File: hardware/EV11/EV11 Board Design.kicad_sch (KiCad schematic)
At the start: 121 parts, among them CN1 PJ-313E-8A_C707222, CN2 X1270WVS-2X05B-6TV01, CN3 WAFER-SH1.0-6PWB, CN4 WAFER-SH1.0-6PWB, CN5 Conn_05x02_Male, CN6 Conn_05x02_Male, CN7 Conn_05x02_Male, J1 Conn_01x02_Socket, J10 Conn_01x08_Socket, J9 USB_C_Receptacle, SW1 TS-1037-A11B3-D2, SW3 TS-1037-A11B3-D2, SW4 SW_Push, SW5 SW_Push, SW6 SW_SPDT, U1 STM32F405RGTx, U11 ESP32-S3-WROOM-1-N8R2, U13 BM14B(0.8)-24DS-0.4V(53), U3 CH340C, U4 USBLC6-2P6, U5 M24C02-RMN6TP, U6 WM8960CGEFL/RV, U7 TPS63060, U8 STM32F072C8T6, U9 BQ21040DBV, Y1 Crystal_GND24

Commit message: Updated vias to be .6mm/.3mm. Added Analog plane. Added more debug connectors
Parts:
- removed CN1: PJ-313E-8A_C707222, PJ-313E-8A:AUDIO-SMD_PJ-313E-8A-EH, symbol PJ-313E-8A:PJ-313E-8A_C707222
- removed U11: ESP32-S3-WROOM-1-N8R2, RF_Module:ESP32-S3-WROOM-1U, symbol ESP32-S3-WROOM-1-N8R2:ESP32-S3-WROOM-1-N8R2
- removed U8: STM32F072C8T6, STM32F072C8T6:LQFP-48_L7.0-W7.0-P0.50-LS9.0-BL, symbol STM32F072C8T6:STM32F072C8T6
- added C21, C22, C27, C56: 100n, Capacitor_SMD:C_0402_1005Metric, symbol Device:C
- added C33, C52: 4u7, Capacitor_SMD:C_0402_1005Metric, symbol Device:C
- added C49, C50: 1u, Capacitor_SMD:C_0402_1005Metric, symbol Device:C
- added C51, C55: 4.7u, Capacitor_SMD:C_0402_1005Metric, symbol Device:C
- added C53, C54: 100u, Capacitor_SMD:C_1206_3216Metric, symbol Device:C
- added J2: AudioJack1, Connector_Audio:Jack_3.5mm_PJ320D_Horizontal, symbol Connector_Audio:AudioJack4
- added J3: Conn_01x06_Socket, Connector_JST:JST_SHL_SM06B-SHLS-TF_1x06-1MP_P1.00mm_Horizontal, symbol Connector:Conn_01x06_Socket
- added JP2: SolderJumper_2_Bridged, NetTie:NetTie-2_SMD_Pad0.5mm, symbol Jumper:SolderJumper_2_Bridged
- added NT1: NetTie_4, NetTie:NetTie-4_SMD_Pad0.5mm, symbol Device:NetTie_4
- added R42: 0R1, Resistor_SMD:R_0603_1608Metric, symbol Device:R_US
- added R43: 2k2, Resistor_SMD:R_0402_1005Metric, symbol Device:R_US
- added TP1, TP2: TestPoint, TestPoint:TestPoint_THTPad_D1.5mm_Drill0.7mm, symbol Connector:TestPoint
- added U11: ESP32-S3-WROOM-1-N8R2, RF_Module:ESP32-S3-WROOM-1U, symbol RF_Module:ESP32-S3-WROOM-1
- added U8: STM32F070CBTx, Package_QFP:LQFP-48_7x7mm_P0.5mm, symbol MCU_ST_STM32F0:STM32F070CBTx
- added U9: WM8960CGEFL/RV, Package_DFN_QFN:QFN-32-1EP_5x5mm_P0.5mm_EP3.45x3.45mm_ThermalVias, symbol Hactar_Symbols:WM8960CGEFL/RV_1
- CN2: value X1270WVS-2X05B-6TV01 -> Conn_05x02_Female; footprint X1270WVS-2x05B-6TV01:IDC-SMD_10P-P1.27_X1270WVS-2X05B-6TV01 -> Hactar_Footprints:IDC-SMD_10P-P1.27_X1270WVS-2X05B-6TV01; symbol X1270WVS-2x05B-6TV01:X1270WVS-2X05B-6TV01 -> Connector_Generic:Conn_02x05_Odd_Even
- CN3, CN4: value WAFER-SH1.0-6PWB -> Conn_01x06_Female; footprint WAFER-SH1.0-6PWB:CONN-SMD_6P-P1.00_XUNPU_WAFER-SH1.0-6PWB -> Connector_JST:JST_SHL_SM06B-SHLS-TF_1x06-1MP_P1.00mm_Horizontal; symbol WAFER-SH1.0-6PWB:WAFER-SH1.0-6PWB -> Connector:Conn_01x06_Socket
- CN5, CN6, CN7: value Conn_05x02_Male -> Conn_02x05_Male; footprint X1270WVS-2x05B-6TV01:IDC-SMD_10P-P1.27_X1270WVS-2X05B-6TV01 -> Hactar_Footprints:IDC-SMD_10P-P1.27_X1270WVS-2X05B-6TV01; symbol X1270WVS-2x05B-6TV01:X1270WVS-2X05B-6TV01 -> Connector_Generic:Conn_02x05_Odd_Even
- D3, D4, D5, D7: footprint NH-B1515RGBA-HF:LED-ARRAY-SMD_4P-L1.6-W1.5-TL_NH-B1515RGBA -> Hactar_Footprints:LED-ARRAY-SMD_4P-L1.6-W1.5-TL_NH-B1515RGBA; symbol NH-B1515RGBA-HF:NH-B1515RGBA-HF -> Hactar_Symbols:NH-B1515RGBA-HF
- L1: footprint MCL2016A1R0MT:L0806 -> Hactar_Footprints:MCL2016A1R0MT
- R11, R12, R15, R17, R18, R24, R25: value 150 -> 150R
- R16, R23: value 180 -> 180R
- R35: footprint Resistor_SMD:R_0603_1608Metric -> Resistor_SMD:R_0402_1005Metric; JLCPCB Part # C4211 -> C25784
- SW1, SW3: footprint TS-1037-A11B3-D2:KEY-SMD_2P-L7.1-W10.6-P4.00-LS9.0 -> Hactar_Footprints:KEY-SMD_2P-L7.1-W10.6-P4.00-LS9.0; symbol TS-1037-A11B3-D2:TS-1037-A11B3-D2 -> Switch:SW_Push
- SW6: footprint (none) -> Button_Switch_THT:SW_E-Switch_EG1224_SPDT_Angled; JLCPCB Part # (none) -> C273395; JLCPCB Position Offset (none) -> 0.1, 4.1
- U13: footprint BM14B(0.B)-24DS-0:BM14B(0.B)-24DS-0.4V(53) -> Hactar_Footprints:BM14B(0.B)-24DS-0.4V(53); symbol Keyboard Symbol:BM14B(0.8)-24DS-0.4V(53) -> Hactar_Symbols:BM14B(0.8)-24DS-0.4V(53)
- U6: footprint Package_DFN_QFN:QFN-32-1EP_5x5mm_P0.5mm_EP3.3x3.3mm_ThermalVias -> Package_DFN_QFN:QFN-32-1EP_5x5mm_P0.5mm_EP3.45x3.45mm_ThermalVias; symbol Audio Interface:WM8960CGEFL/RV -> Hactar_Symbols:WM8960CGEFL/RV_1
- renumbered U9 to U2
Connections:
- net +3.3V: now also C24.2, C25.2, C26.2, CN5.1 (Pin_1), CN6.1 (Pin_1), SW4.1, U1.1 (VBAT), C21.2, C22.2, C56.1, J3.1 (Pin_1), U11.2 (3V3), U8.1 (VDD), U8.24 (VDD), U8.36 (VDD), U8.48 (VDD), U8.9 (VDDA), U9.10 (DBVDD), U9.8 (DCVDD); no longer C24.1, C25.1, C26.1, CN5.8, CN6.8, SW4.2
- net +3.3VA: now also C27.2, C33.1, C52.1, U9.21 (SPKVDD2), U9.26 (SPKVDD1), U9.32 (AVDD)
- net BOOT1: now also U8.45 (PB8)
- net GND: now also C24.1, C25.1, C26.1, C35.2, CN5.3 (Pin_3), CN6.3 (Pin_3), R2.1, R3.1, R32.2, SW5.1, C21.1, C22.1, C51.2, C55.2, C56.2, J3.6 (Pin_6), JP2.2 (B), NT1.1, NT1.3, U11.1 (GND), U11.40 (GND), U11.41 (GND), U8.23 (VSS), U8.35 (VSS), U8.47 (VSS), U8.8 (VSSA), U9.20 (SPKGND2), U9.24 (SPKGND1), U9.28 (AGND), U9.33 (EP), U9.9 (DGND); no longer C24.2, C25.2, C26.2, C28.2, C3.2, C31.1, C35.1, C6.2, C7.1, C8.2, C9.2, CN5.10, CN6.10, JP1.2 (B), R2.2, R3.2, R32.1, SW5.2, U6.20 (SPKGND2), U6.24 (SPKGND1), U6.28 (AGND), U6.33 (EP)
- net HP_L: now also C53.2, J2.T
- net HP_R: now also C54.2, J2.R1
- net I2S_ADCDAT: now also CN5.10 (Pin_10), U9.16 (ADCDAT); no longer CN5.5
- net I2S_BCLK: now also CN5.7 (Pin_7), U9.12 (BCLK); no longer CN5.3
- net I2S_DACDAT: now also CN5.8 (Pin_8), U9.14 (DACDAT); no longer CN5.7
- net I2S_DACLRC: now also CN5.9 (Pin_9), U9.13 (DACLRC); no longer CN5.1
- net LEDA_B: now also U8.17 (PA7)
- net LEDA_G: now also U8.16 (PA6)
- net LEDA_R: now also U8.14 (PA4)
- net LEDB_B: now also U8.28 (PB15)
- net LEDB_G: now also U8.27 (PB14)
- net LEDB_R: now also U8.18 (PB0)
- net MCLK: now also CN5.2 (Pin_2), U8.29 (PA8), U9.11 (MCLK); no longer CN5.9
- net MGMT_BOOT: now also SW4.2, U8.44 (BOOT0); no longer SW4.1
- net MGMT_NRST: now also C35.1, SW5.2, U8.7 (NRST); no longer C35.2, SW5.1
- net MGMT_SWCLK: now also U8.37 (PA14)
- net MGMT_SWDIO: now also U8.34 (PA13)
- net MIC_N: now also C5.2, C50.1, J2.R2, JP2.1 (A); no longer C5.1
- net MIC_P: now also C18.2, R9.1, C49.1, J2.S, R43.2; no longer C18.1, R9.2
- net NET_BOOT: now also J3.5 (Pin_5), U11.27 (IO0), U8.41 (PB5)
- net NET_DEBUG_1: now also U11.7 (IO7)
- net NET_DEBUG_2: now also U11.8 (IO15)
- net NET_DEBUG_3: now also U11.9 (IO16)
- net NET_LED_B: now also U11.29 (IO36)
- net NET_LED_G: now also U11.30 (IO37)
- net NET_LED_R: now also U11.31 (IO38)
- net NET_MTCK: now also CN2.6 (Pin_6), U11.32 (IO39); no longer CN2.4
- net NET_MTDI: now also CN2.2 (Pin_2), U11.34 (IO41); no longer CN2.8
- net NET_MTDO: now also CN2.4 (Pin_4), U11.33 (IO40); no longer CN2.6
- net NET_MTMS: now also CN2.8 (Pin_8), U11.35 (IO42); no longer CN2.2
- net NET_NRST: now also J3.2 (Pin_2), U11.3 (EN), U8.40 (PB4)
- net NET_RX1_MGMT: now also CN6.8 (Pin_8), J3.3 (Pin_3), U11.36 (RXD0), U8.21 (PB10); no longer CN6.7
- net NET_STAT: now also U11.23 (IO21), U8.11 (PA1)
- net NET_TX1_MGMT: now also CN6.10 (Pin_10), J3.4 (Pin_4), U11.37 (TXD0), U8.22 (PB11); no longer CN6.9
- net RCC_OSC_IN: now also U8.5 (PF0)
- net RCC_OSC_OUT: now also U8.6 (PF1)
- net UI_BOOT: now also U8.39 (PB3)
- net UI_DEBUG_1: now also U1.44 (PA11); no longer U1.20 (PA4)
- net UI_DEBUG_3: now also U1.20 (PA4); no longer U1.44 (PA11)
- net UI_LED_G: now also R25.1; no longer R24.1
- net UI_LED_R: now also R24.1; no longer R25.1
- net UI_NRST: now also U8.38 (PA15)
- net UI_RX1_MGMT: now also CN6.4 (Pin_4), U8.12 (PA2); no longer CN6.3
- net UI_RX2_NET: now also CN6.7 (Pin_7), U11.10 (IO17); no longer CN6.4
- net UI_SCL: now also CN5.6 (Pin_6), U9.17 (SCLK); no longer CN5.2
- net UI_SDA: now also U9.18 (SDIN)
- net UI_STAT: now also U8.10 (PA0)
- net UI_TX1_MGMT: now also CN6.6 (Pin_6), U8.13 (PA3); no longer CN6.5
- net UI_TX2_NET: now also CN6.5 (Pin_5), U11.11 (IO18); no longer CN6.2
- net USB_CC1_DETECT: now also U1.11 (PC3); no longer U1.10 (PC2)
- net USB_CC2_DETECT: now also U1.10 (PC2); no longer U1.11 (PC3)
- net USB_DTR: now also U8.26 (PB13)
- net USB_RTS: now also U8.19 (PB1)
- net USB_RX1_MGMT: now also CN6.2 (Pin_2), U8.30 (PA9); no longer CN6.1
- net USB_TX1_MGMT: now also CN6.9 (Pin_9), U8.31 (PA10); no longer CN6.6
- net at R36.2: now also CN7.6 (Pin_6); no longer CN7.5
- net at U6.4 (LINPUT1): now also C5.1; no longer C5.2
- net at D7.1 (-): now also R24.2; no longer R25.2
- net at D7.4 (-): now also R25.2; no longer R24.2
- net at R38.2: now also CN7.10 (Pin_10); no longer CN7.1
- net at C37.1, C38.1, C39.1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: now also R42.2, TP2.1; no longer D2.1 (K), D6.1 (K)
- net at C28.1, U6.1 (MICBIAS): now also R9.2; no longer R9.1
- net at U6.27 (AMID): now also C31.1; no longer C31.2
- net at U6.3 (LINPUT2): now also C18.1; no longer C18.2
- net at R41.2: now also CN7.9 (Pin_9); no longer CN7.10
- net at CN7.3 (Pin_3): no longer R37.2
- net at R39.2: now also CN7.5 (Pin_5); no longer CN7.6
- net at CN7.7 (Pin_7): now also R40.2
- net at CN7.8 (Pin_8): now also R37.2; no longer R40.2
- net PG: no longer names the net of R21.1, U7.5 (PG)
- net UD+: no longer names the net of U4.6 (I/O1)
- net UD+: now also J9.A7 (D-), J9.B7 (D-); no longer U3.5 (UD+)
- net UD-: no longer names the net of U4.4 (I/O2)
- net UD-: now also J9.A6 (D+), J9.B6 (D+); no longer U3.6 (UD-)
- removed net USB_D+: J9.A6 (D+), J9.B6 (D+), U4.1 (I/O1)
- removed net USB_D-: J9.A7 (D-), J9.B7 (D-), U4.3 (I/O2)
- new net: C54.1, U9.29 (HP_R)
- new net: C51.1, R43.1, U9.1 (MICBIAS)
- new net: D2.1 (K), D6.1 (K), R42.1, TP1.1
- new net: C50.2, U9.4 (LINPUT1)
- new net: J9.A5 (CC1), R3.2, R31.2
- new net: J9.B5 (CC2), R2.2, R33.2
- new net: R32.1, U11.16 (IO46)
- new net: C27.1, C33.2, C52.2
- new net: C55.1, U9.27 (AMID)
- new net: C49.2, U9.3 (LINPUT2)
- new net: C53.1, U9.31 (HP_L)
- new net: U3.6 (UD-), U4.1 (I/O1)
- new net: U3.5 (UD+), U4.3 (I/O2)
- new net GNDA: C28.2, C3.2, C31.2, C6.2, C7.1, C8.2, C9.2, JP1.2 (B), NT1.2, NT1.4, U6.20 (SPKGND2), U6.24 (SPKGND1), U6.28 (AGND), U6.33 (EP)
- no-connect marks 70 -> 69
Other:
- note added: "1 Capacitor Per Voltage Pin Not including VBAT"
- note added: "AFFECTS BOOTLOADER"
- note added: "Chip boot mode"
- note added: "JUST HERE FOR REVIEW"
- moved on the sheet: C1, C10, C11, C12, C13, C14, C15, C16, C17, C18, C19, C20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

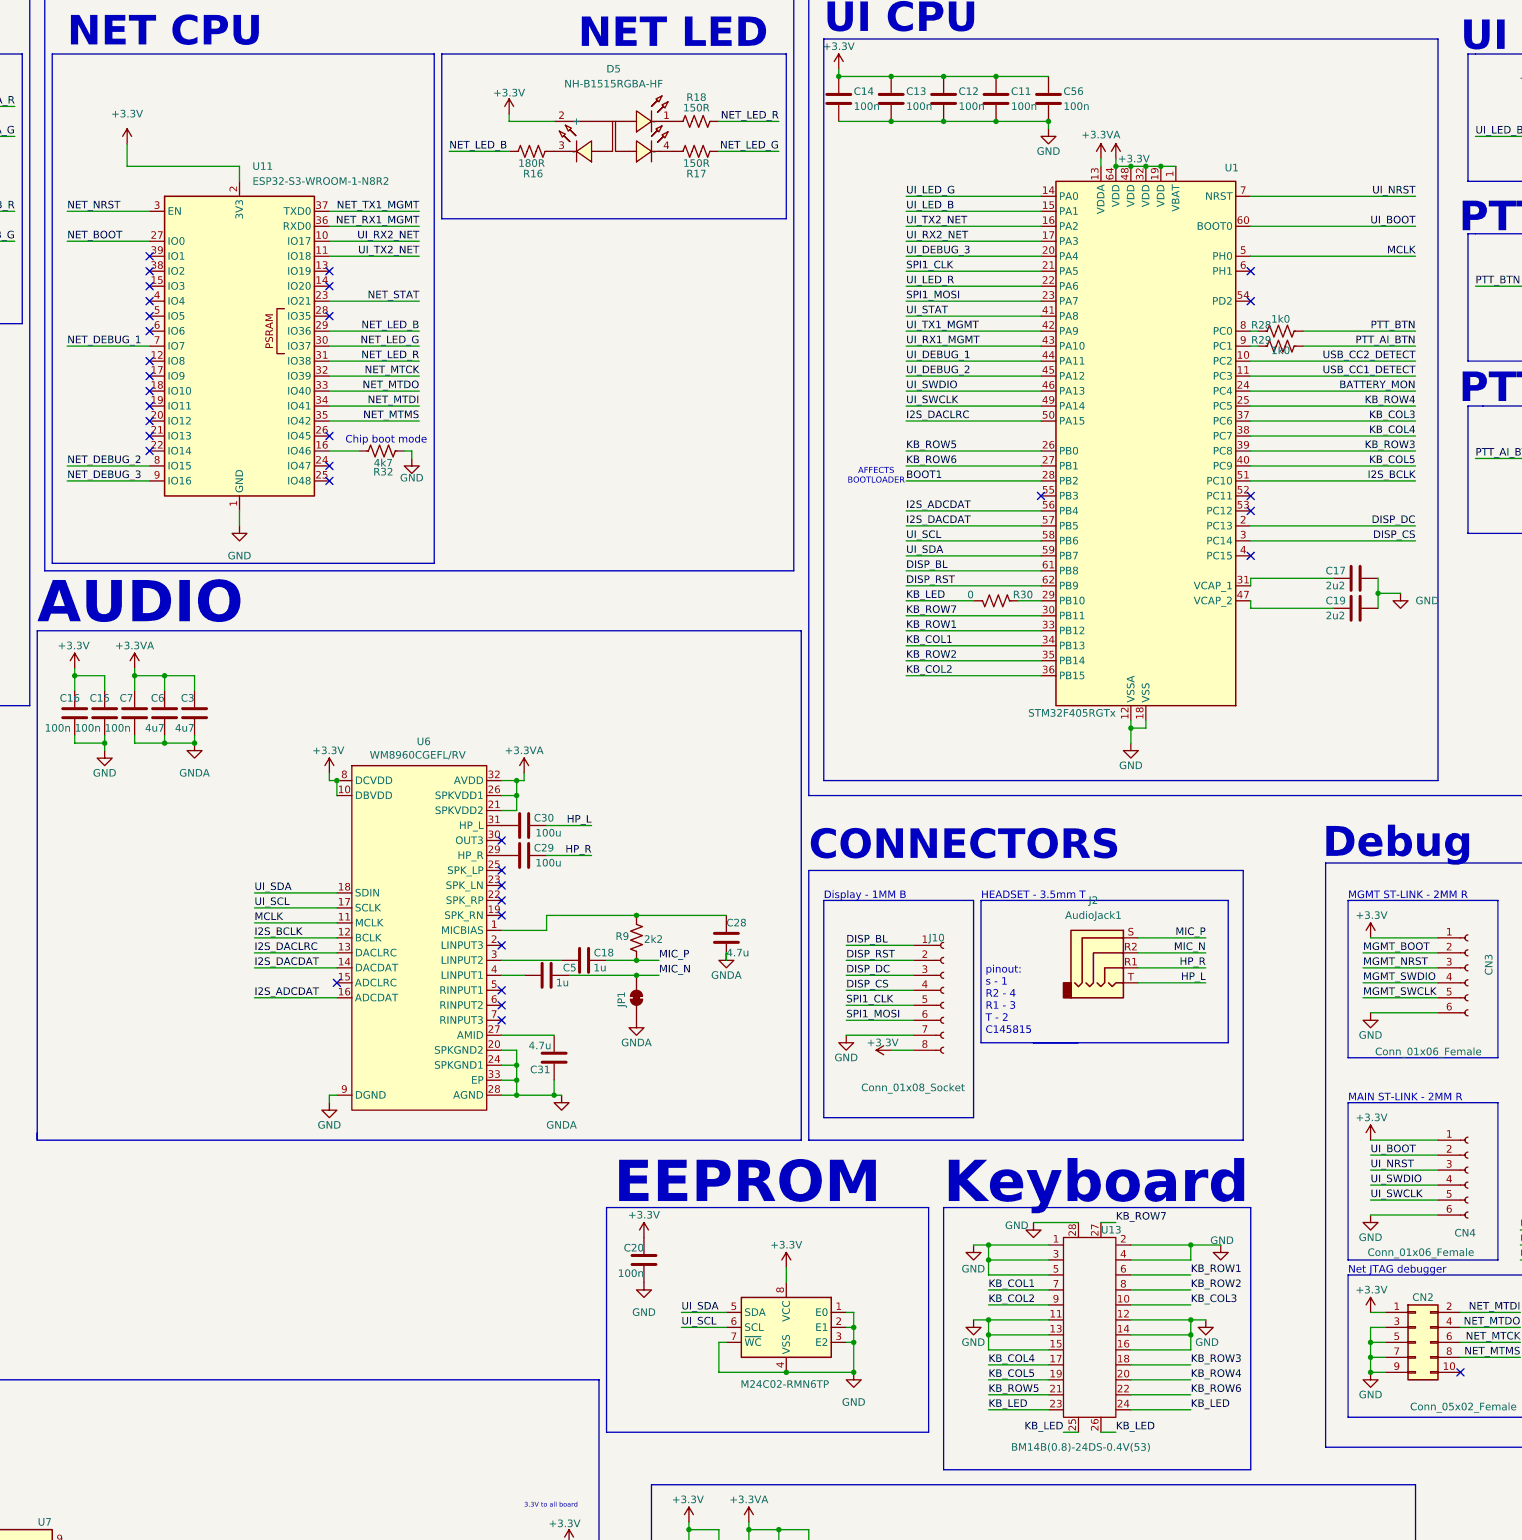
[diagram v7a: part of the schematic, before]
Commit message: Added agnd and mic ouput to wm8960 RINPUT1
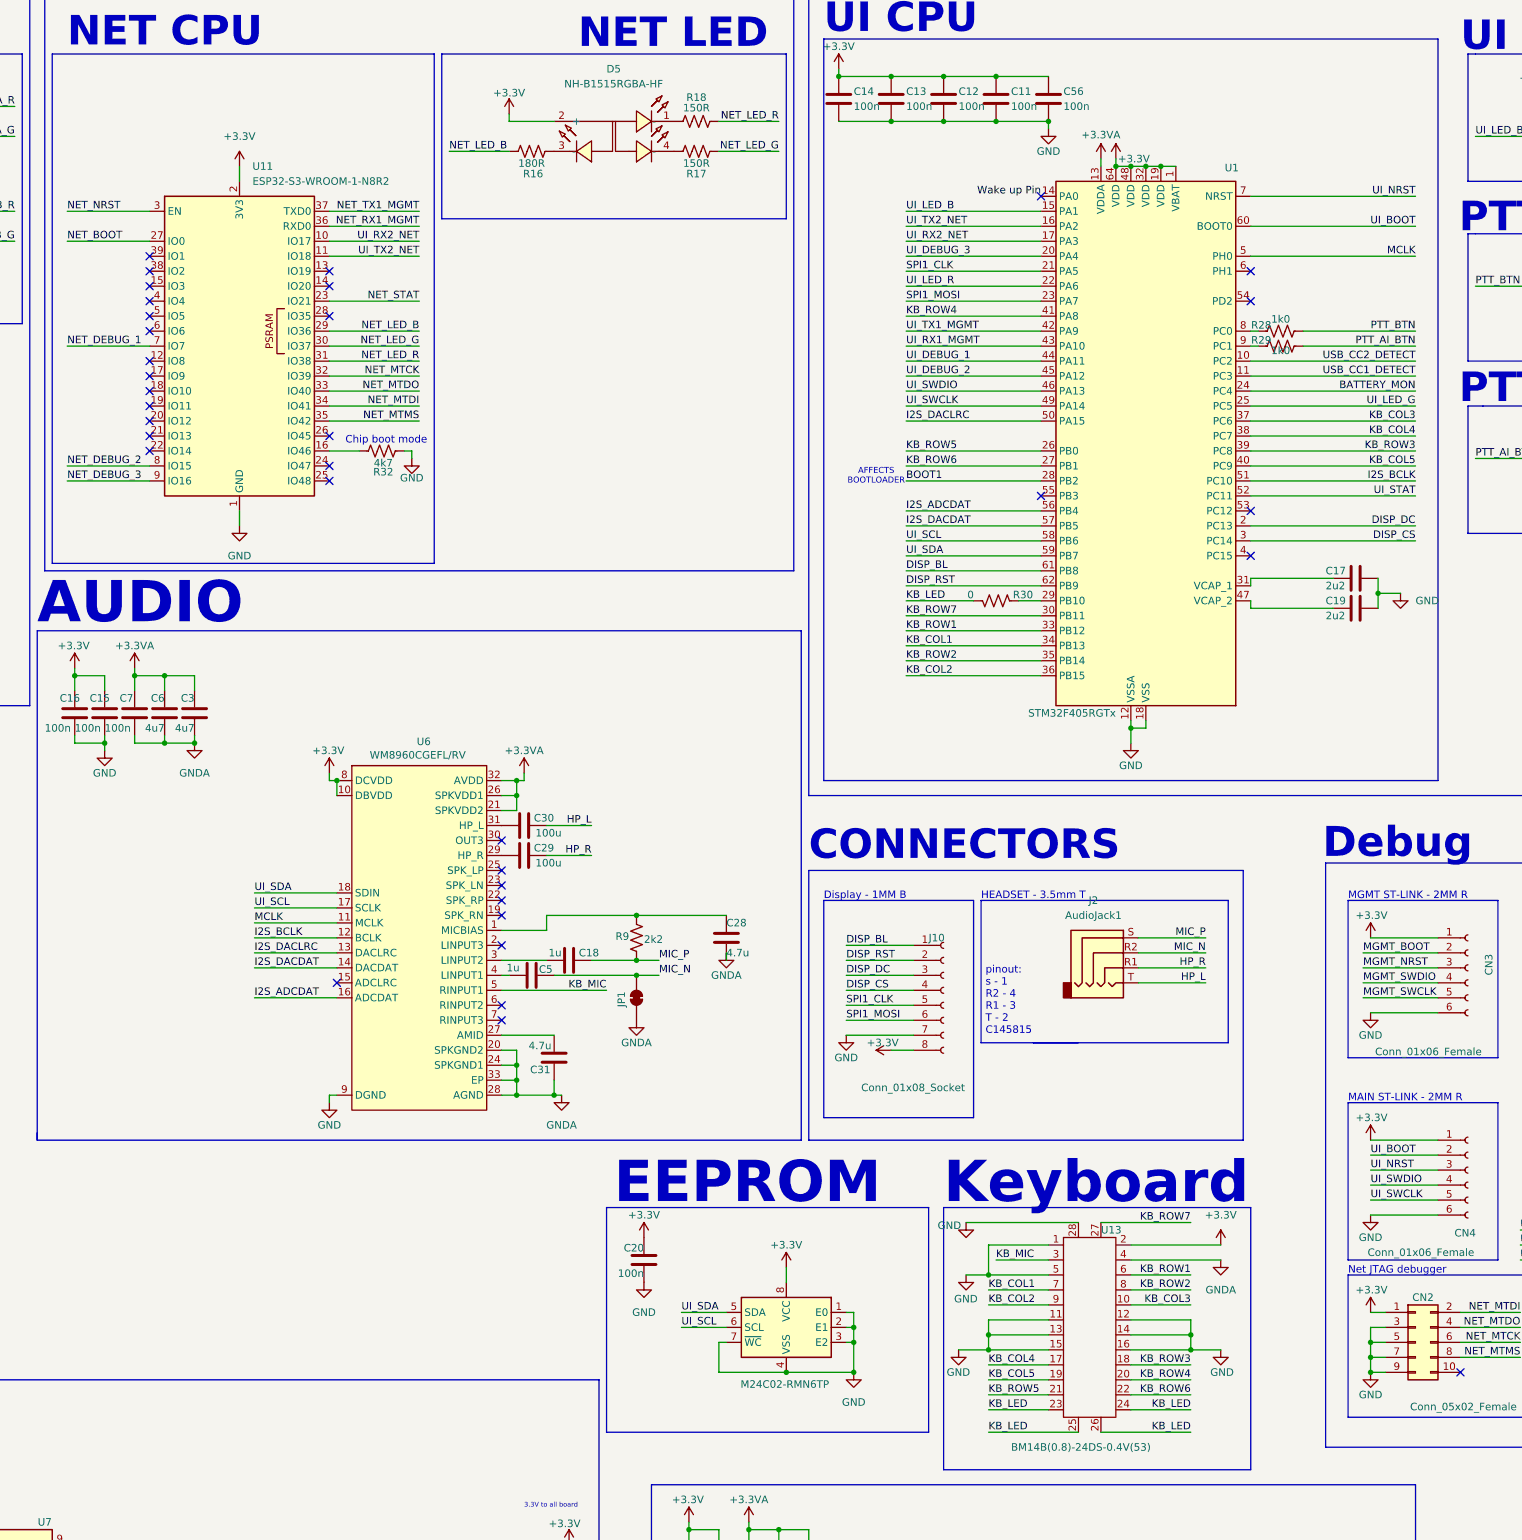
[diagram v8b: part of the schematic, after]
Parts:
- U13: footprint Hactar_Footprints:BM14B(0.B)-24DS-0.4V(53) -> BM14B(0.B)-24DS-0:BM14B(0.B)-24DS-0.4V(53)
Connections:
- net +3.3V: now also U13.2
- net GND: no longer U13.2, U13.3, U13.4
- net GNDA: now also U13.4
- net KB_ROW4: now also U1.41 (PA8); no longer U1.25 (PC5)
- net UI_LED_G: now also U1.25 (PC5); no longer U1.14 (PA0)
- net UI_STAT: now also U1.52 (PC11); no longer U1.41 (PA8)
- net KB_MIC: now reaches U6.5 (RINPUT1)
- net KB_MIC: now also U13.3
- new net Wake up Pin: U1.14 (PA0)
- no-connect marks 69 -> 68
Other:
- moved on the sheet: C18, C5
